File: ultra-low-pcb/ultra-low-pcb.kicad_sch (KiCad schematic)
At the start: 31 parts, among them IC1 ESP32-C3-WROOM-02-N4, IC2 TPS2117DRLR, J1 USB_C_Receptacle_USB2.0, J2 S2B-PH-SM4-TB_LF__SN_, Q1 AO3401A, SW1 TC-0522C-1.7-160G, SW2 TC-0522C-1.7-160G, SW3 TC-0522C-1.7-160G, U1 USBLC6-2P6, U2 MCP1700-3302E_SOT23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

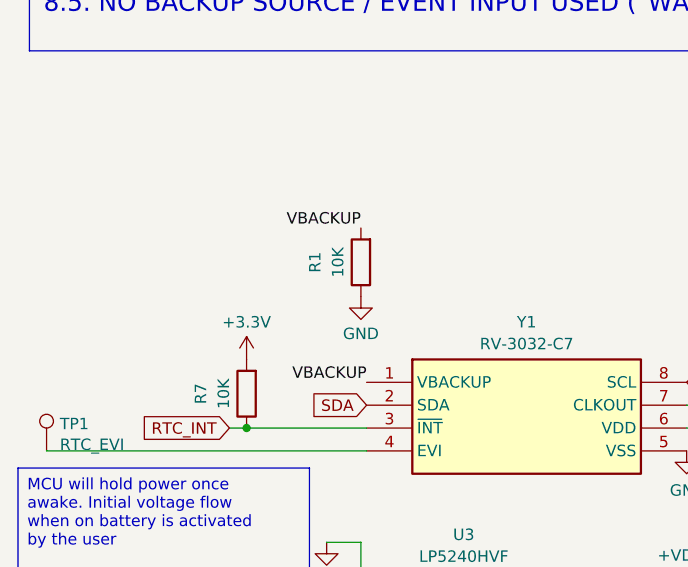
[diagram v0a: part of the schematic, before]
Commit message: Add SuperCAP to RTC
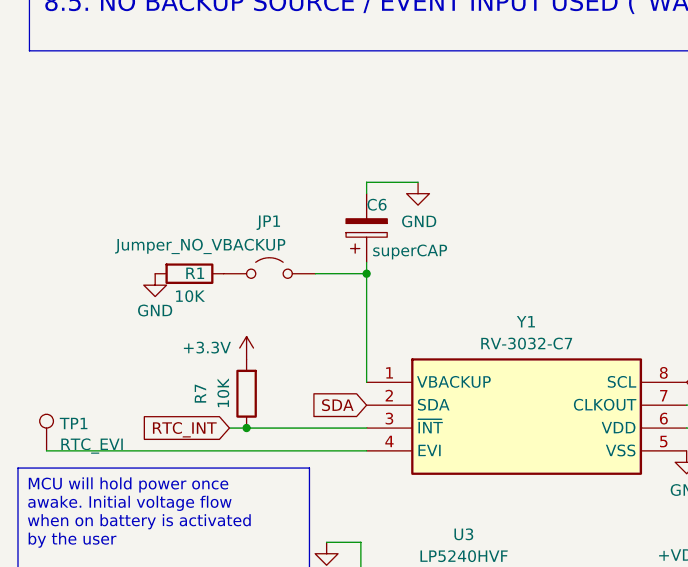
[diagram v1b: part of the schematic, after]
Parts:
- added C6: superCAP, footprint:C9900013866_SUPERCAP-TH_XH414HG, symbol Device:C_Polarized
- added JP1: Jumper_NO_VBACKUP, symbol Jumper:Jumper_2_Open
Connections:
- net GND: now also R1.2, C6.2; no longer R1.1
- net VBACKUP: no longer names the net of Y1.1 (VBACKUP)
- net VBACKUP: now also C6.1, JP1.2 (B); no longer R1.2
- new net: JP1.1 (A), R1.1
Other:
- moved on the sheet: R1

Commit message: Update schematics
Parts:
- removed R10: 5.1k, Resistor_SMD:R_0603_1608Metric, symbol Device:R
- added C7, C8: 10uF, Capacitor_SMD:C_0805_2012Metric, symbol Device:C
- added D1: Schottky, Diode_SMD:D_SOD-123, symbol Device:D_Small
- added U6: L78L33ACUTR, Package_TO_SOT_SMD:SOT-89-3, symbol epaper-breakout-rescue:MCP1700-3302E_SOT23-Regulator_Linear
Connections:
- net +3.3V: no longer C5.1
- net GND: now also C7.1, C8.1, U6.1 (GND)
- net MCU_PWRHOLD: now also D1.2 (A); no longer R11.1, U3.B2 (EN)
- net VIN: now also C8.2, U6.3 (VI)
- net +3.3VP: now reaches SW3.1, SW3.2
- net +3.3VP: now also C5.1, C7.2, U6.2 (VO)
- new net: D1.1 (K), R11.1, U3.B2 (EN)
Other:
- note added: "49dB@(120Hz) 100mA Fixed 3.3V low dropout LDO"
- moved on the sheet: C3, C4, IC2, J2, R4, R5, R6, R8, R9, SW1, SW2, SW3

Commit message: Correct C5
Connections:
- net +3.3VP: now also Y1.6 (VDD)
- net GND: now also C5.2
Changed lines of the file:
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@@
 	)
 	(junction
+		(at 102.235 77.47)
+		(diameter 0)
+		(color 0 0 0 0)
+	)
+	(junction
 		(at 157.48 165.1)
 		(diameter 0)
@@
 	(wire
 		(pts
-			(xy 107.315 77.47) (xy 94.615 77.47)
+			(xy 137.16 165.1) (xy 140.335 165.1)
 		)
 		(stroke
@@
 	(wire
 		(pts
-			(xy 137.16 165.1) (xy 140.335 165.1)
+			(xy 58.42 90.17) (xy 58.42 95.885)
 		)
 		(stroke
@@
 		)
 	)
-	(wire
+	(polyline
 		(pts
-			(xy 58.42 90.17) (xy 58.42 95.885)
+			(xy 224.79 94.615) (xy 224.79 114.935)
 		)
 		(stroke
@@
 		)
 	)
-	(polyline
+	(wire
 		(pts
-			(xy 224.79 94.615) (xy 224.79 114.935)
+			(xy 178.435 90.17) (xy 178.435 92.71)
 		)
 		(stroke
@@
 	(wire
 		(pts
-			(xy 178.435 90.17) (xy 178.435 92.71)
+			(xy 105.41 77.47) (xy 102.235 77.47)
 		)
 		(stroke
@@
 	(wire
 		(pts
+			(xy 102.235 77.47) (xy 94.615 77.47)
+		)
+		(stroke
+			(width 0)
+			(type default)
+		)
+	)
+	(wire
+		(pts
 			(xy 93.98 98.425) (xy 78.74 98.425)
 		)
@@
 	)
 	(symbol
-		(lib_id "power:+3.3VP")
-		(at 107.315 69.85 0)
-		(unit 1)
-		(exclude_from_sim no)
-		(in_bom yes)
-		(on_board yes)
-		(dnp no)
-		(property "Reference" "PWR_RTC"
-			(at 112.395 68.58 0)
-			(effects
-				(font
-					(size 1.27 1.27)
-				)
-			)
-		)
-		(property "Value" "+3.3VP"
-			(at 107.315 65.7169 0)
-			(effects
-				(font
-					(size 1.27 1.27)
-				)
-			)
-		)
-		(property "Footprint" ""
-			(at 107.315 69.85 0)
-			(effects
-				(font
-					(size 1.27 1.27)
-				)
-				(hide yes)
-			)
-		)
-		(property "Datasheet" ""
-			(at 107.315 69.85 0)
-			(effects
-				(font
-					(size 1.27 1.27)
-				)
-				(hide yes)
-			)
-		)
-		(property "Description" "Power symbol creates a global label with name \"+3.3VP\""
-			(at 107.315 69.85 0)
-			(effects
-				(font
-					(size 1.27 1.27)
-				)
-				(hide yes)
-			)
-		)
-		(pin "1"
-		)
-		(instances
-			(project ""
-				(path "/5ee1aa4e-e444-4714-9002-fd9f67b16fcd"
-					(reference "PWR_RTC")
-					(unit 1)
-				)
-			)
-		)
-	)
-	(symbol
 		(lib_id "power:GND")
 		(at 64.77 50.165 0)
@@
 	(symbol
 		(lib_id "power:GND")
+		(at 102.235 85.09 0)
+		(unit 1)
+		(exclude_from_sim no)
+		(in_bom yes)
+		(on_board yes)
+		(dnp no)
+		(property "Reference" "#PWR21"
+			(at 102.235 91.44 0)
+			(effects
+				(font
+					(size 1.27 1.27)
+				)
+				(hide yes)
+			)
+		)
+		(property "Value" "GND"
+			(at 102.362 89.4842 0)
+			(effects
+				(font
+					(size 1.27 1.27)
+				)
+			)
+		)
+		(property "Footprint" ""
+			(at 102.235 85.09 0)
+			(effects
+				(font
+					(size 1.27 1.27)
+				)
+				(hide yes)
+			)
+		)
+		(property "Datasheet" ""
+			(at 102.235 85.09 0)
+			(effects
+				(font
+					(size 1.27 1.27)
+				)
+				(hide yes)
+			)
+		)
+		(property "Description" ""
+			(at 102.235 85.09 0)
+			(effects
+				(font
+					(size 1.27 1.27)
+				)
+				(hide yes)
+			)
+		)
+		(pin "1"
+		)
+		(instances
+			(project "ultra-low-pcb"
+				(path "/5ee1aa4e-e444-4714-9002-fd9f67b16fcd"
+					(reference "#PWR21")
+					(unit 1)
+				)
+			)
+		)
+	)
+	(symbol
+		(lib_id "power:GND")
 		(at 199.39 41.275 0)
 		(mirror y)
@@
 	)
 	(symbol
-		(lib_id "Device:C")
-		(at 107.315 73.66 0)
-		(unit 1)
-		(exclude_from_sim no)
-		(in_bom yes)
-		(on_board yes)
-		(dnp no)
-		(property "Reference" "C5"
-			(at 106.045 76.2 0)
-			(effects
-				(font
-					(size 1.27 1.27)
-				)
-				(justify right)
-			)
-		)
-		(property "Value" "100nF"
-			(at 114.935 71.12 0)
-			(effects
-				(font
-					(size 1.27 1.27)
-				)
-				(justify right)
-			)
-		)
-		(property "Footprint" "Capacitor_SMD:C_0805_2012Metric"
-			(at 108.2802 77.47 0)
-			(effects
-				(font
-					(size 1.27 1.27)
-				)
-				(hide yes)
-			)
-		)
-		(property "Datasheet" "~"
-			(at 107.315 73.66 0)
-			(effects
-				(font
-					(size 1.27 1.27)
-				)
-				(hide yes)
-			)
-		)
-		(property "Description" ""
-			(at 107.315 73.66 0)
-			(effects
-				(font
-					(size 1.27 1.27)
-				)
-				(hide yes)
-			)
-		)
-		(property "LCSC" "C49678"
-			(at 107.315 73.66 0)
-			(effects
-				(font
-					(size 1.27 1.27)
-				)
-				(hide yes)
-			)
-		)
-		(pin "1"
-		)
-		(pin "2"
-		)
-		(instances
-			(project "ultra-low-pcb"
-				(path "/5ee1aa4e-e444-4714-9002-fd9f67b16fcd"
-					(reference "C5")
-					(unit 1)
-				)
-			)
-		)
-	)
-	(symbol
 		(lib_id "Connector:TestPoint")
 		(at 23.495 80.01 0)
@@
 	)
 	(symbol
+		(lib_id "power:+3.3VP")
+		(at 105.41 77.47 0)
+		(unit 1)
+		(exclude_from_sim no)
+		(in_bom yes)
+		(on_board yes)
+		(dnp no)
+		(property "Reference" "PWR_RTC1"
+			(at 111.76 76.835 0)
+			(effects
+				(font
+					(size 1.27 1.27)
+				)
+			)
+		)
+		(property "Value" "+3.3VP"
+			(at 105.41 73.3369 0)
+			(effects
+				(font
+					(size 1.27 1.27)
+				)
+			)
+		)
+		(property "Footprint" ""
+			(at 105.41 77.47 0)
+			(effects
+				(font
+					(size 1.27 1.27)
+				)
+				(hide yes)
+			)
+		)
+		(property "Datasheet" ""
+			(at 105.41 77.47 0)
+			(effects
+				(font
+					(size 1.27 1.27)
+				)
+				(hide yes)
+			)
+		)
+		(property "Description" "Power symbol creates a global label with name \"+3.3VP\""
+			(at 105.41 77.47 0)
+			(effects
+				(font
+					(size 1.27 1.27)
+				)
+				(hide yes)
+			)
+		)
+		(pin "1"
+		)
+		(instances
+			(project "ultra-low-pcb"
+				(path "/5ee1aa4e-e444-4714-9002-fd9f67b16fcd"
+					(reference "PWR_RTC1")
+					(unit 1)
+				)
+			)
+		)
+	)
+	(symbol
 		(lib_id "Device:R")
 		(at 52.07 107.315 270)
@@
 					(unit 1)
 				)
+			)
+		)
+	)
+	(symbol
+		(lib_id "Device:C")
+		(at 102.235 81.28 0)
+		(unit 1)
+		(exclude_from_sim no)
+		(in_bom yes)
+		(on_board yes)
+		(dnp no)
+		(property "Reference" "C5"
+			(at 100.965 83.82 0)
+			(effects
+				(font
+					(size 1.27 1.27)
+				)
+				(justify right)
+			)
+		)
+		(property "Value" "100nF"
+			(at 102.235 78.74 0)
+			(effects
+				(font
+					(size 1.27 1.27)
+				)
+				(justify right)
+			)
+		)
+		(property "Footprint" "Capacitor_SMD:C_0805_2012Metric"
+			(at 103.2002 85.09 0)
+			(effects
+				(font
+					(size 1.27 1.27)
+				)
+				(hide yes)
+			)
+		)
+		(property "Datasheet" "~"
+			(at 102.235 81.28 0)
+			(effects
+				(font
+					(size 1.27 1.27)
+				)
+				(hide yes)
+			)
+		)
+		(property "Description" ""
+			(at 102.235 81.28 0)
+			(effects
+				(font
+					(size 1.27 1.27)
+				)
+				(hide yes)
+			)
+		)
+		(property "LCSC" "C49678"
+			(at 102.235 81.28 0)
+			(effects
+				(font
+					(size 1.27 1.27)
+				)
+				(hide yes)
+			)
+		)
+		(pin "1"
+		)
+		(pin "2"
+		)
+		(instances
+			(project "ultra-low-pcb"
+				(path "/5ee1aa4e-e444-4714-9002-fd9f67b16fcd"
+					(reference "C5")
+					(unit 1)
+				)

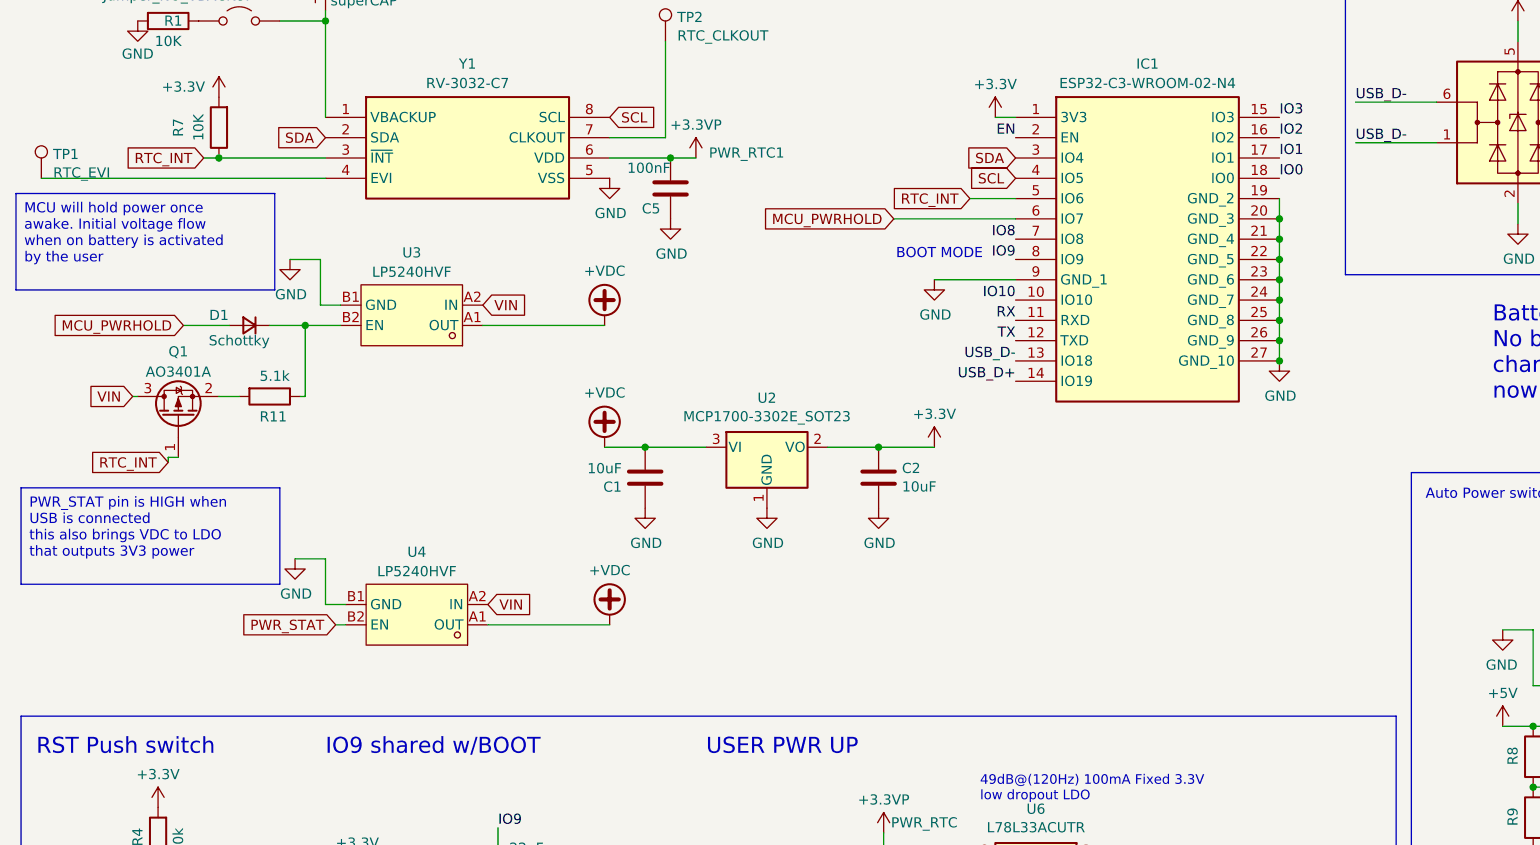
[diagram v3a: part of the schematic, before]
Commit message: Add EVI app PWR up
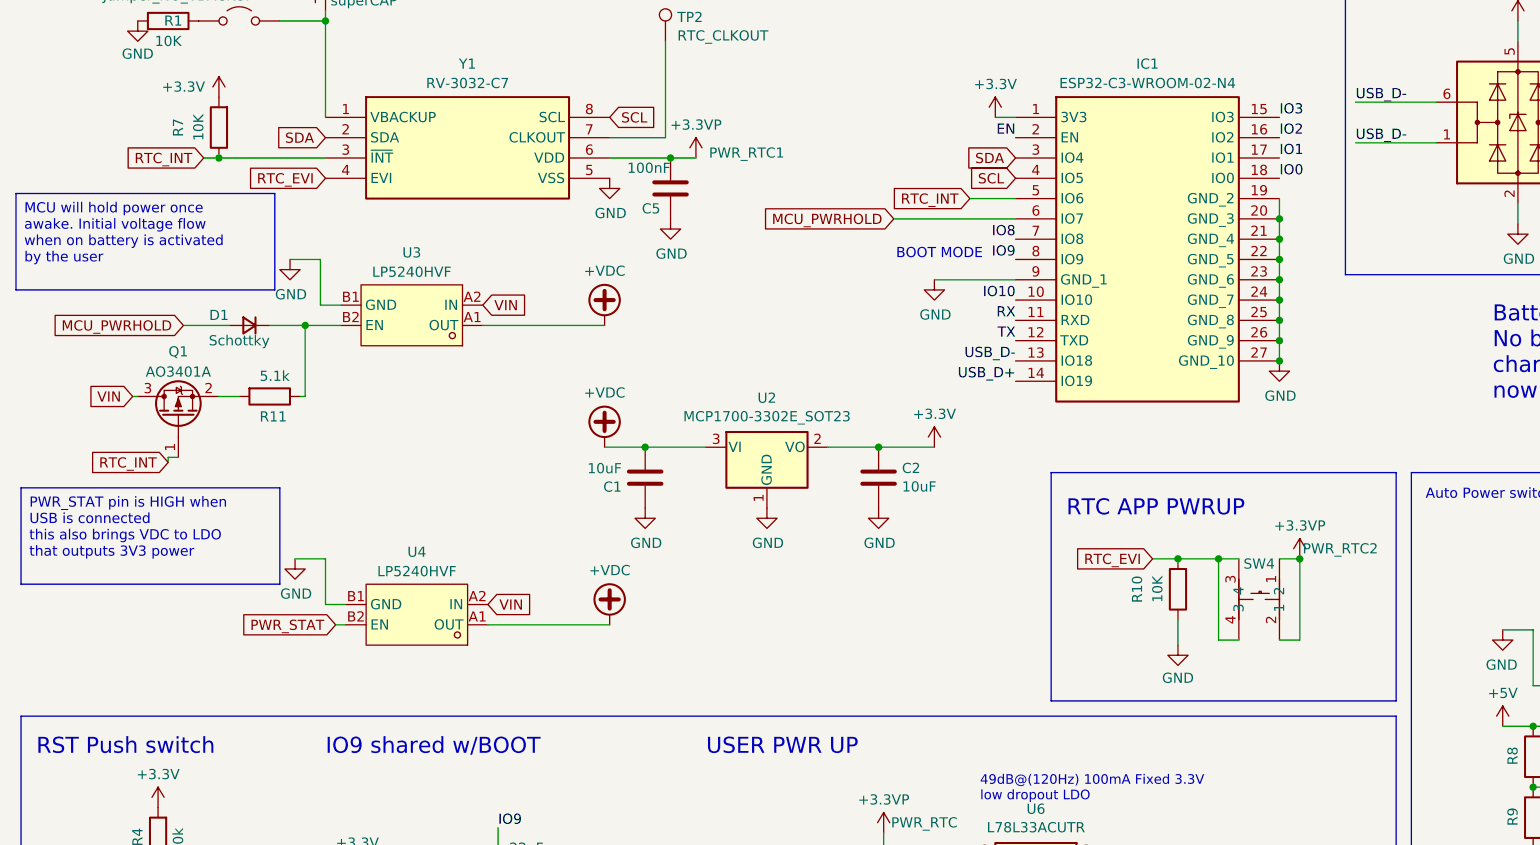
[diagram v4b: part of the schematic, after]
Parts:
- removed TP1: RTC_EVI, TestPoint:TestPoint_Pad_D1.5mm, symbol Connector:TestPoint
- added R10: 10K, Resistor_SMD:R_0603_1608Metric, symbol Device:R
- added SW4: TC-0522C-1.7-160G, footprints:C2845289_SW-SMD_4P-L5.2-W5.2-P3.70-LS6.4, symbol BUTTON:TC-0522C-1.7-160G
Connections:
- net +3.3VP: now also SW4.1, SW4.2
- net GND: now also R10.1
- net RTC_EVI: now reaches Y1.4 (EVI)
- net RTC_EVI: now also R10.2, SW4.3, SW4.4
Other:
- note added: "RTC APP PWRUP"

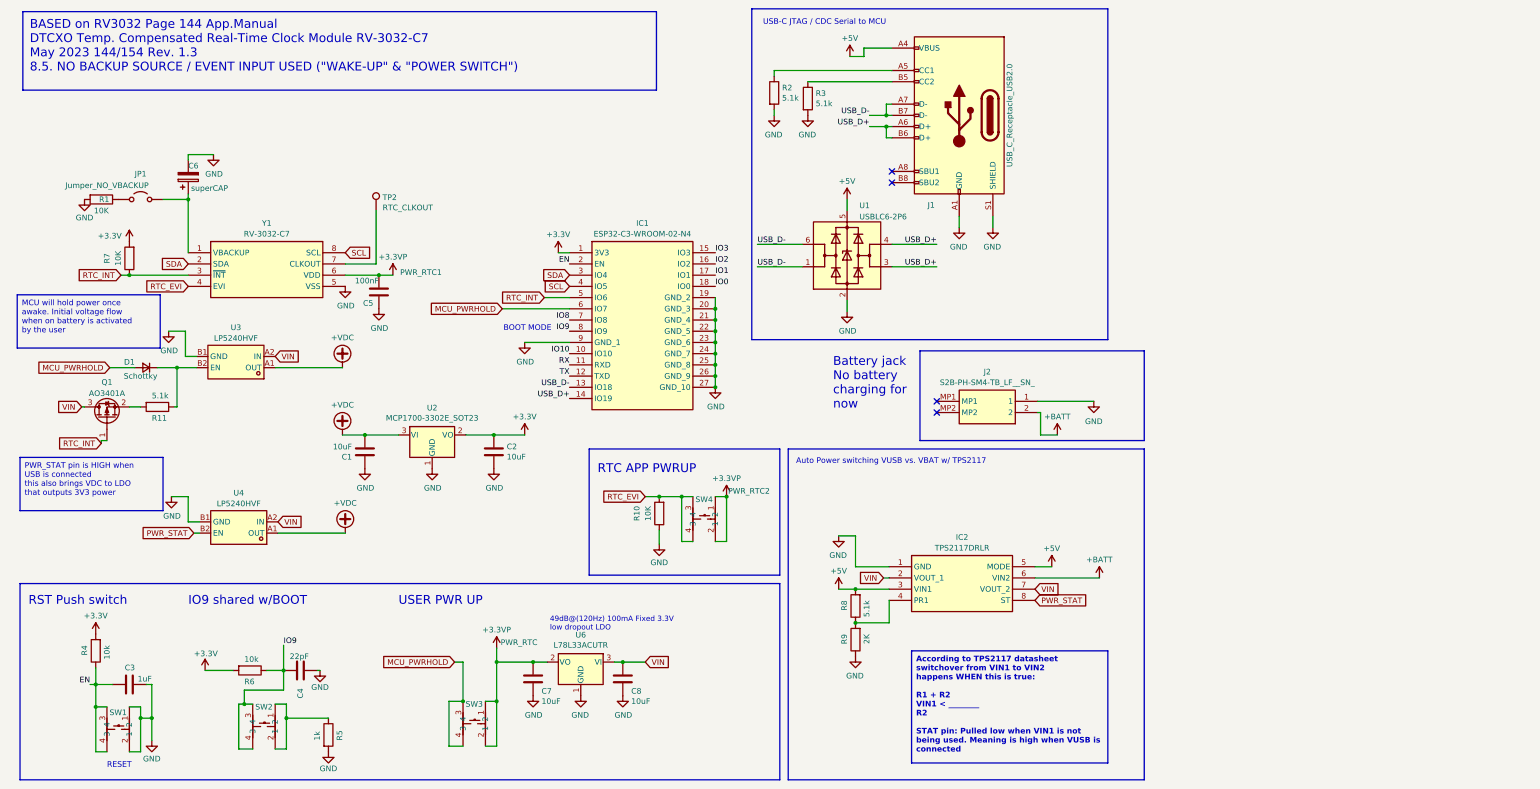
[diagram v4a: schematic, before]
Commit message: 1.0 passes DRC
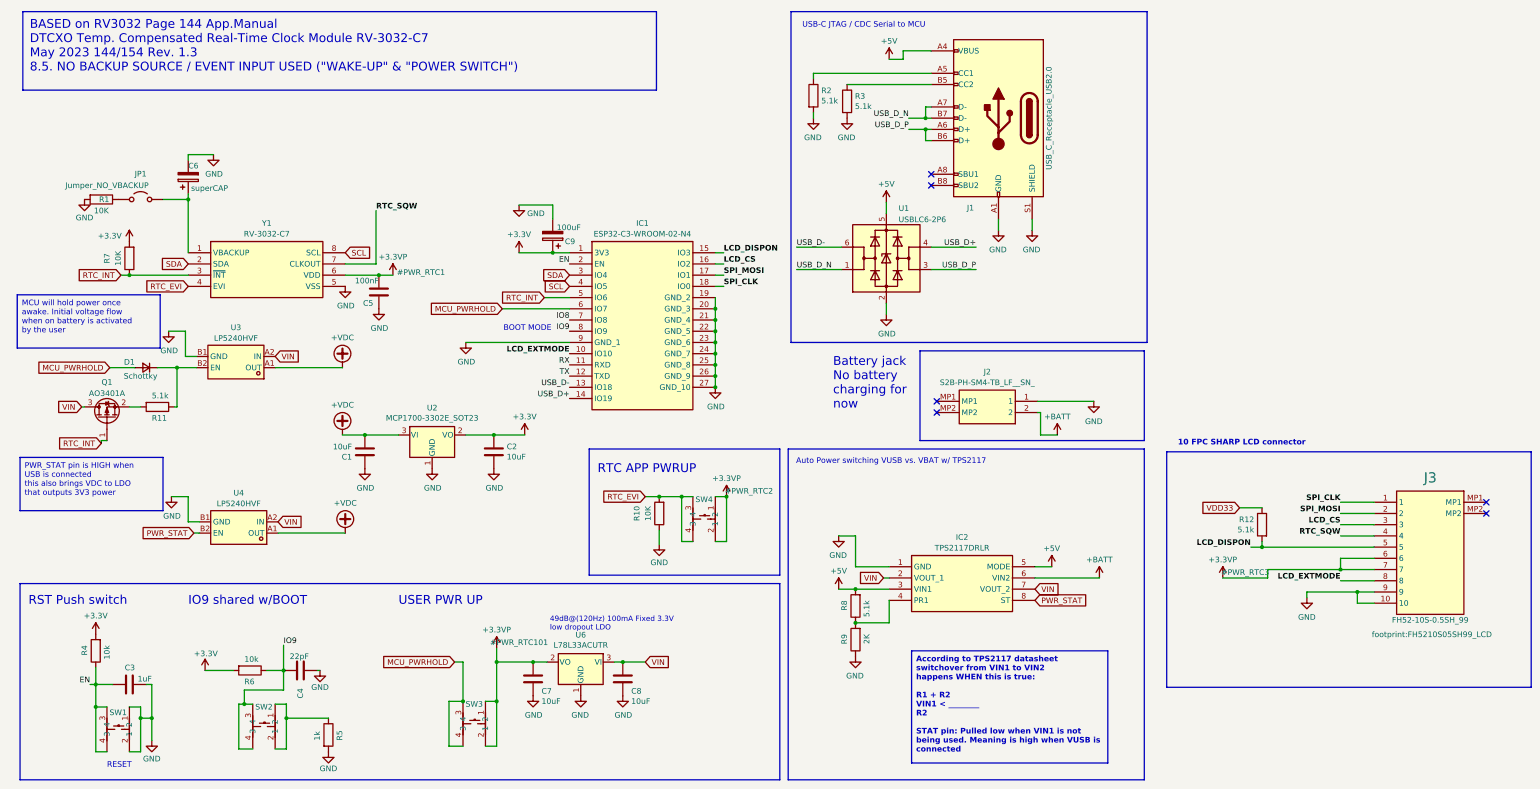
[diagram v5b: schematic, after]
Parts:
- removed TP2: RTC_CLKOUT, TestPoint:TestPoint_Pad_D1.5mm, symbol Connector:TestPoint
- added C9: 100uF, Capacitor_Tantalum_SMD:CP_EIA-3528-15_AVX-H, symbol Device:C_Polarized
- added J3: FH52-10S-0.5SH_99, footprint:FH5210S05SH99_LCD, symbol 10_FPC:FH52-10S-0.5SH_99_
- added R12: 5.1k, Resistor_SMD:R_0603_1608Metric, symbol Device:R
- IC2: footprint footprints:C22399676_TPS2117-8N -> footprint:C22399676_TPS2117-8N
- JP1: footprint (none) -> Jumper:SolderJumper-2_P1.3mm_Open_RoundedPad1.0x1.5mm
- R5: footprint Resistor_SMD:R_0402_1005Metric -> Resistor_SMD:R_0603_1608Metric
- SW1, SW2, SW3, SW4: footprint footprints:C2845289_SW-SMD_4P-L5.2-W5.2-P3.70-LS6.4 -> footprint:C2845289_SW-SMD_4P-L5.2-W5.2-P3.70-LS6.4
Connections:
- net +3.3V: now also C9.1
- net +3.3VP: now also J3.6, J3.7
- net GND: now also C9.2, J3.10, J3.9
- net USB_D+: no longer J1.A6 (D+), J1.B6 (D+), U1.3 (I/O2)
- net USB_D-: no longer J1.A7 (D-), J1.B7 (D-), U1.1 (I/O1)
- net RTC_SQW: now reaches Y1.7 (CLKOUT)
- net RTC_SQW: now also J3.4
- net IO0 renamed SPI_CLK
- net SPI_CLK: now also J3.1
- net IO1 renamed SPI_MOSI
- net SPI_MOSI: now also J3.2
- net IO10 renamed LCD_EXTMODE
- net LCD_EXTMODE: now also J3.8
- net IO2 renamed LCD_CS
- net LCD_CS: now also J3.3
- net IO3 renamed LCD_DISPON
- net LCD_DISPON: now also J3.5, R12.2
- new net USB_D_N: J1.A7 (D-), J1.B7 (D-), U1.1 (I/O1)
- new net USB_D_P: J1.A6 (D+), J1.B6 (D+), U1.3 (I/O2)
- new net VDD33: R12.1
- no-connect marks 4 -> 6
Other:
- note added: "10 FPC SHARP LCD connector"
- moved on the sheet: J1, R2, R3, U1

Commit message: Update U3
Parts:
- added R13: 0Ω, Resistor_SMD:R_0603_1608Metric, symbol Device:R
- R11: value 5.1k -> 10k; LCSC C23186 -> C25804
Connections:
- net GND: now also R11.2
- net at D1.1 (K), R11.1, U3.B2 (EN): now also R13.2
- net at Q1.2 (S): now also R13.1; no longer R11.2
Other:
- moved on the sheet: U3

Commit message: Correct Q1. Thanks Syl!
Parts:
- added R14: ${SIM.PARAMS}, Resistor_SMD:R_0603_1608Metric, symbol Device:R
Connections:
- net +3.3V: no longer R7.2
- net +3.3VP: now also R7.2
- net RTC_EVI: now also R14.1, R14.2
- net VIN: now also Q1.2 (S); no longer Q1.3 (D)
- net at R13.1: now also Q1.3 (D); no longer Q1.2 (S)
